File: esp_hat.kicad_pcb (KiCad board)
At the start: 2 copper layers, 73 x 30 mm, 111 parts, among them J1 U.FL, P1 CONN_02X20, U1 ESP8266EX, U2 AP1117D33, Y1 26MHz

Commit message: v0.2 fab files
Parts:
- added REF**: Symbol_OSHW-Logo_SilkScreen, Symbols:Symbol_OSHW-Logo_SilkScreen, F.Cu at (91.1, 109.5)
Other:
- board text added: "ESP8266 WiFi for Raspberry Pi v0.2 2015-12-31 by Andrew Litt https://github.com/al177/esp_hat"
- board text added: "NO STEP"
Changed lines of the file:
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@@
 (kicad_pcb (version 4) (host pcbnew 4.0.1-3.201512221401+6198~38~ubuntu15.10.1-stable)
   (general
-    (links 220)
+    (links 0)
     (no_connects 2)
     (area 56.924999 84.924999 130.075001 115.075001)
     (thickness 1.6)
-    (drawings 11)
+    (drawings 13)
     (tracks 504)
     (zones 0)
-    (modules 111)
+    (modules 112)
     (nets 30)
   )
   (page A4)
   (title_block
-    (title WiFiPiPants)
+    (title "ESP8266 WiFi for Raspberry Pi")
     (date 2015-12-31)
     (rev v0.2)
@@
       (net 1 GND))
   )
+  (module Symbols:Symbol_OSHW-Logo_SilkScreen (layer F.Cu)
+    (at 91.1 109.5)
+    (descr "Symbol, OSHW-Logo, Silk Screen,")
+    (tags "Symbol, OSHW-Logo, Silk Screen,")
+    (fp_text reference REF** (at 0.09906 -4.38912) (layer F.SilkS) hide
+      (effects (font (size 1 1) (thickness 0.15)))
+    )
+    (fp_text value Symbol_OSHW-Logo_SilkScreen (at 0.30988 6.56082) (layer F.Fab)
+      (effects (font (size 1 1) (thickness 0.15)))
+    )
+    (fp_line (start 1.66878 2.68986) (end 2.02946 4.16052) (layer F.SilkS) (width 0.15))
+    (fp_line (start 2.02946 4.16052) (end 2.30886 3.0988) (layer F.SilkS) (width 0.15))
+    (fp_line (start 2.30886 3.0988) (end 2.61874 4.17068) (layer F.SilkS) (width 0.15))
+    (fp_line (start 2.61874 4.17068) (end 2.9591 2.72034) (layer F.SilkS) (width 0.15))
+    (fp_line (start 0.24892 3.38074) (end 1.03886 3.37058) (layer F.SilkS) (width 0.15))
+    (fp_line (start 1.03886 3.37058) (end 1.04902 3.38074) (layer F.SilkS) (width 0.15))
+    (fp_line (start 1.04902 3.38074) (end 1.04902 3.37058) (layer F.SilkS) (width 0.15))
+    (fp_line (start 1.08966 2.65938) (end 1.08966 4.20116) (layer F.SilkS) (width 0.15))
+    (fp_line (start 0.20066 2.64922) (end 0.20066 4.21894) (layer F.SilkS) (width 0.15))
+    (fp_line (start 0.20066 4.21894) (end 0.21082 4.20878) (layer F.SilkS) (width 0.15))
+    (fp_line (start -0.35052 2.75082) (end -0.70104 2.66954) (layer F.SilkS) (width 0.15))
+    (fp_line (start -0.70104 2.66954) (end -1.02108 2.65938) (layer F.SilkS) (width 0.15))
+    (fp_line (start -1.02108 2.65938) (end -1.25984 2.86004) (layer F.SilkS) (width 0.15))
+    (fp_line (start -1.25984 2.86004) (end -1.29032 3.12928) (layer F.SilkS) (width 0.15))
+    (fp_line (start -1.29032 3.12928) (end -1.04902 3.37058) (layer F.SilkS) (width 0.15))
+    (fp_line (start -1.04902 3.37058) (end -0.6604 3.50012) (layer F.SilkS) (width 0.15))
+    (fp_line (start -0.6604 3.50012) (end -0.48006 3.66014) (layer F.SilkS) (width 0.15))
+    (fp_line (start -0.48006 3.66014) (end -0.43942 3.95986) (layer F.SilkS) (width 0.15))
+    (fp_line (start -0.43942 3.95986) (end -0.67056 4.18084) (layer F.SilkS) (width 0.15))
+    (fp_line (start -0.67056 4.18084) (end -0.9906 4.20878) (layer F.SilkS) (width 0.15))
+    (fp_line (start -0.9906 4.20878) (end -1.34112 4.09956) (layer F.SilkS) (width 0.15))
+    (fp_line (start -2.37998 2.64922) (end -2.6289 2.66954) (layer F.SilkS) (width 0.15))
+    (fp_line (start -2.6289 2.66954) (end -2.8702 2.91084) (layer F.SilkS) (width 0.15))
+    (fp_line (start -2.8702 2.91084) (end -2.9591 3.40106) (layer F.SilkS) (width 0.15))
+    (fp_line (start -2.9591 3.40106) (end -2.93116 3.74904) (layer F.SilkS) (width 0.15))
+    (fp_line (start -2.93116 3.74904) (end -2.7305 4.06908) (layer F.SilkS) (width 0.15))
+    (fp_line (start -2.7305 4.06908) (end -2.47904 4.191) (layer F.SilkS) (width 0.15))
+    (fp_line (start -2.47904 4.191) (end -2.16916 4.11988) (layer F.SilkS) (width 0.15))
+    (fp_line (start -2.16916 4.11988) (end -1.95072 3.93954) (layer F.SilkS) (width 0.15))
+    (fp_line (start -1.95072 3.93954) (end -1.8796 3.4798) (layer F.SilkS) (width 0.15))
+    (fp_line (start -1.8796 3.4798) (end -1.9304 3.07086) (layer F.SilkS) (width 0.15))
+    (fp_line (start -1.9304 3.07086) (end -2.03962 2.78892) (layer F.SilkS) (width 0.15))
+    (fp_line (start -2.03962 2.78892) (end -2.4003 2.65938) (layer F.SilkS) (width 0.15))
+    (fp_line (start -1.78054 0.92964) (end -2.03962 1.49098) (layer F.SilkS) (width 0.15))
+    (fp_line (start -2.03962 1.49098) (end -1.50114 2.00914) (layer F.SilkS) (width 0.15))
+    (fp_line (start -1.50114 2.00914) (end -0.98044 1.7399) (layer F.SilkS) (width 0.15))
+    (fp_line (start -0.98044 1.7399) (end -0.70104 1.89992) (layer F.SilkS) (width 0.15))
+    (fp_line (start 0.73914 1.8796) (end 1.06934 1.6891) (layer F.SilkS) (width 0.15))
+    (fp_line (start 1.06934 1.6891) (end 1.50876 2.0193) (layer F.SilkS) (width 0.15))
+    (fp_line (start 1.50876 2.0193) (end 1.9812 1.52908) (layer F.SilkS) (width 0.15))
+    (fp_line (start 1.9812 1.52908) (end 1.69926 1.04902) (layer F.SilkS) (width 0.15))
+    (fp_line (start 1.69926 1.04902) (end 1.88976 0.57912) (layer F.SilkS) (width 0.15))
+    (fp_line (start 1.88976 0.57912) (end 2.49936 0.39116) (layer F.SilkS) (width 0.15))
+    (fp_line (start 2.49936 0.39116) (end 2.49936 -0.28956) (layer F.SilkS) (width 0.15))
+    (fp_line (start 2.49936 -0.28956) (end 1.94056 -0.42926) (layer F.SilkS) (width 0.15))
+    (fp_line (start 1.94056 -0.42926) (end 1.7399 -1.00076) (layer F.SilkS) (width 0.15))
+    (fp_line (start 1.7399 -1.00076) (end 2.00914 -1.47066) (layer F.SilkS) (width 0.15))
+    (fp_line (start 2.00914 -1.47066) (end 1.53924 -1.9812) (layer F.SilkS) (width 0.15))
+    (fp_line (start 1.53924 -1.9812) (end 1.02108 -1.71958) (layer F.SilkS) (width 0.15))
+    (fp_line (start 1.02108 -1.71958) (end 0.55118 -1.92024) (layer F.SilkS) (width 0.15))
+    (fp_line (start 0.55118 -1.92024) (end 0.381 -2.46126) (layer F.SilkS) (width 0.15))
+    (fp_line (start 0.381 -2.46126) (end -0.30988 -2.47904) (layer F.SilkS) (width 0.15))
+    (fp_line (start -0.30988 -2.47904) (end -0.5207 -1.9304) (layer F.SilkS) (width 0.15))
+    (fp_line (start -0.5207 -1.9304) (end -0.9398 -1.76022) (layer F.SilkS) (width 0.15))
+    (fp_line (start -0.9398 -1.76022) (end -1.49098 -2.02946) (layer F.SilkS) (width 0.15))
+    (fp_line (start -1.49098 -2.02946) (end -2.00914 -1.50114) (layer F.SilkS) (width 0.15))
+    (fp_line (start -2.00914 -1.50114) (end -1.76022 -0.96012) (layer F.SilkS) (width 0.15))
+    (fp_line (start -1.76022 -0.96012) (end -1.9304 -0.48006) (layer F.SilkS) (width 0.15))
+    (fp_line (start -1.9304 -0.48006) (end -2.47904 -0.381) (layer F.SilkS) (width 0.15))
+    (fp_line (start -2.47904 -0.381) (end -2.4892 0.32004) (layer F.SilkS) (width 0.15))
+    (fp_line (start -2.4892 0.32004) (end -1.9304 0.5207) (layer F.SilkS) (width 0.15))
+    (fp_line (start -1.9304 0.5207) (end -1.7907 0.91948) (layer F.SilkS) (width 0.15))
+    (fp_line (start 0.35052 0.89916) (end 0.65024 0.7493) (layer F.SilkS) (width 0.15))
+    (fp_line (start 0.65024 0.7493) (end 0.8509 0.55118) (layer F.SilkS) (width 0.15))
+    (fp_line (start 0.8509 0.55118) (end 1.00076 0.14986) (layer F.SilkS) (width 0.15))
+    (fp_line (start 1.00076 0.14986) (end 1.00076 -0.24892) (layer F.SilkS) (width 0.15))
+    (fp_line (start 1.00076 -0.24892) (end 0.8509 -0.59944) (layer F.SilkS) (width 0.15))
+    (fp_line (start 0.8509 -0.59944) (end 0.39878 -0.94996) (layer F.SilkS) (width 0.15))
+    (fp_line (start 0.39878 -0.94996) (end -0.0508 -1.00076) (layer F.SilkS) (width 0.15))
+    (fp_line (start -0.0508 -1.00076) (end -0.44958 -0.89916) (layer F.SilkS) (width 0.15))
+    (fp_line (start -0.44958 -0.89916) (end -0.8509 -0.55118) (layer F.SilkS) (width 0.15))
+    (fp_line (start -0.8509 -0.55118) (end -1.00076 -0.09906) (layer F.SilkS) (width 0.15))
+    (fp_line (start -1.00076 -0.09906) (end -0.94996 0.39878) (layer F.SilkS) (width 0.15))
+    (fp_line (start -0.94996 0.39878) (end -0.70104 0.70104) (layer F.SilkS) (width 0.15))
+    (fp_line (start -0.70104 0.70104) (end -0.35052 0.89916) (layer F.SilkS) (width 0.15))
+    (fp_line (start -0.35052 0.89916) (end -0.70104 1.89992) (layer F.SilkS) (width 0.15))
+    (fp_line (start 0.35052 0.89916) (end 0.7493 1.89992) (layer F.SilkS) (width 0.15))
+  )
+  (gr_text "NO STEP" (at 60.5 97.5 90) (layer F.SilkS)
+    (effects (font (size 1.5 1.5) (thickness 0.375)))
+  )
+  (gr_text "ESP8266 WiFi for Raspberry Pi\nv0.2 2015-12-31\nby Andrew Litt\nhttps://github.com/al177/esp_hat" (at 88.01 110.82) (layer B.SilkS)
+    (effects (font (size 1 1) (thickness 0.125)) (justify right mirror))
+  )
   (gr_text "max skew must be <250mil\nvariance as routed is 235mil" (at 94.825 101.225) (layer Cmts.User)

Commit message: Add GPIO5/GPIO6 select pad, fix no-connects, remove paste on option pads
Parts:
- added P2: CH_PD, esp_hat:GS3, F.Cu at (104.5, 93.2)
- R3, R4, R5: footprint Connect:GS2 -> esp_hat:GS2
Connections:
- P1 pad 31: (no net) -> GPIO6
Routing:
- net GPIO6: track 0.00 -> 7.90 mm
- net GPIO5: track 58.7 -> 65.7 mm
- net GND: track 250.6 -> 245.7 mm, vias 56 -> 57
- net /50ohm_ant: track 0.99 -> 2.57 mm
- net /50ohm_ufl: track 0.00 -> 1.20 mm
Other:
- board text added: "GPIO0"
- board text added: "GPIO2"
- board text added: "GPIO5"
- board text added: "GPIO6"
- board text added: "MTDO"

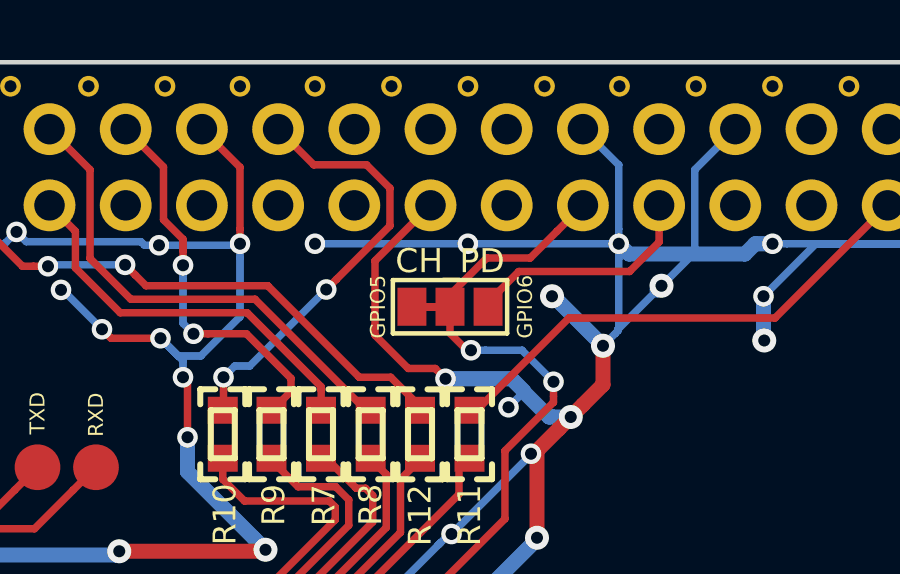
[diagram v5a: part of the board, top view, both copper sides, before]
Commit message: Change CH_PD name to CHIP_EN
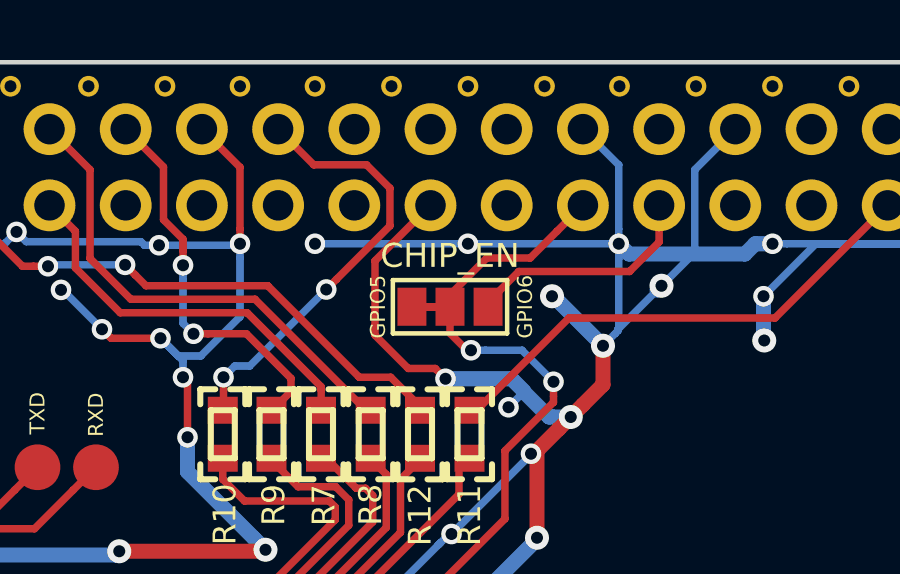
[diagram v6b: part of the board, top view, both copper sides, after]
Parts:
- P2: value CH_PD -> CHIP_EN
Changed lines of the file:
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@@
     (links 223)
     (no_connects 0)
-    (area 56.808999 79.875 134.19881 117.47626)
+    (area 56.924999 84.924999 130.075001 115.075001)
     (thickness 1.6)
     (drawings 18)
@@
     (pad_to_mask_clearance 0.2)
     (aux_axis_origin 0 0)
-    (visible_elements 7FFE7F7F)
+    (visible_elements 7FFFFF7F)
     (pcbplotparams
       (layerselection 0x010f8_80000001)
@@
       (effects (font (size 1 1) (thickness 0.15)))
     )
-    (fp_text value CH_PD (at 1.524 0 180) (layer F.SilkS)
+    (fp_text value CHIP_EN (at 1.7 0 180) (layer F.SilkS)
       (effects (font (size 0.8 0.8) (thickness 0.125)))
     )

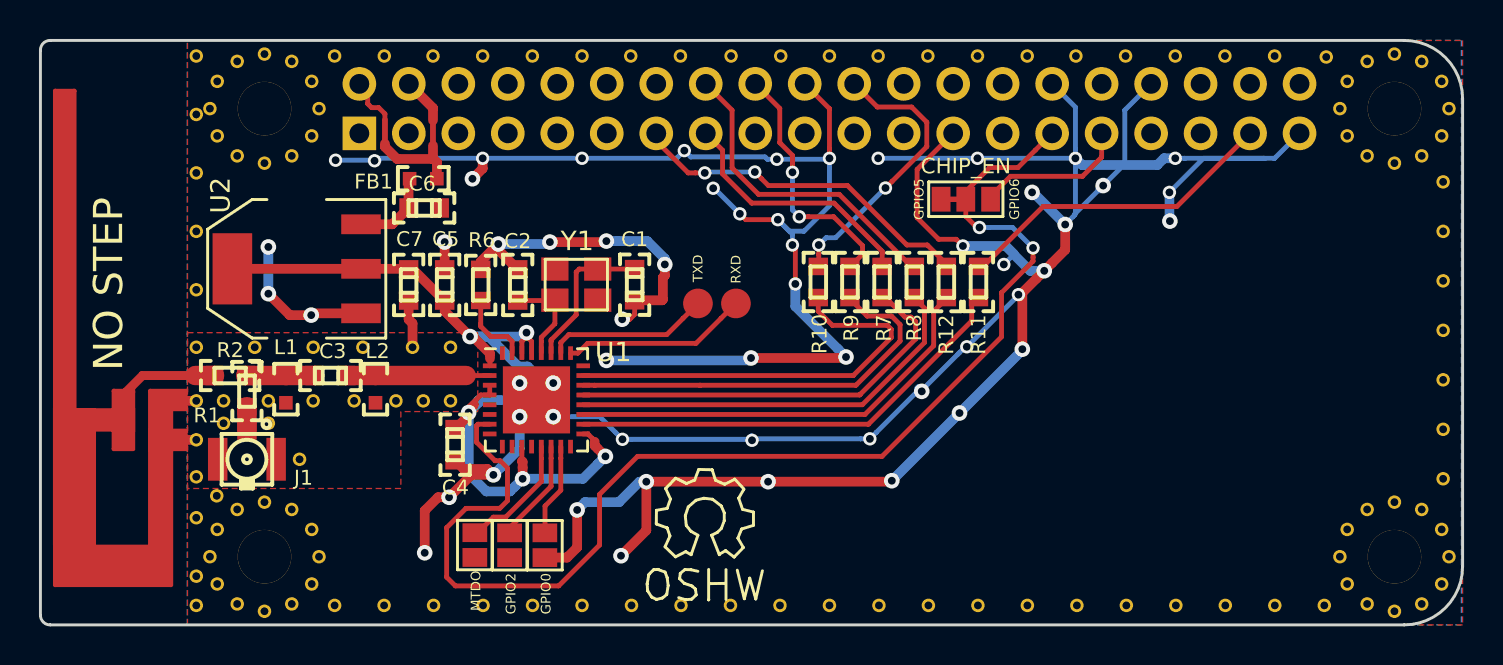
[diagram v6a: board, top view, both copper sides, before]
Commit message: Add part# parameters, clean up refs, set attributes for proper mfg
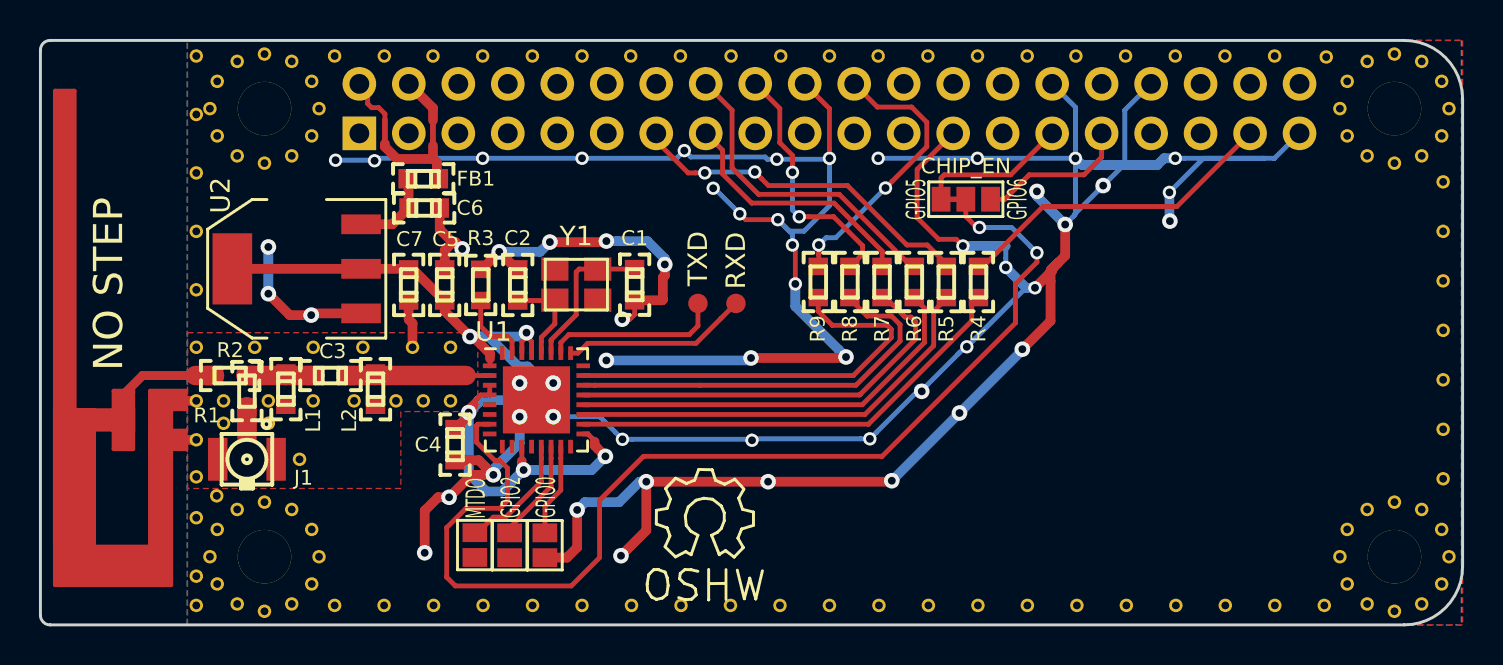
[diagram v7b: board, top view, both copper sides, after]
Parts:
- FB1, L1, L2: footprint mcuos:0603(1608m) -> mcuos:0603(1608m)-CHIP-CAP
- J1: value U.FL -> DNP
- JP2: renamed from R3; value DNP -> MTDO
- JP3: renamed from R4; value DNP -> GPIO2
- JP4: renamed from R5; value DNP -> GPIO0
- R3: renamed from R6; value 12.0K -> 12.0K 1%
- W1, W2: footprint Measurement_Points:Measurement_Point_Round-SMD-Pad_Small -> esp_hat:Measurement_Point_Round-SMD-Pad_Small
- Y1: value 26MHz -> 26MHz 10ppm
- renumbered P2 to JP1, R11 to R4, R12 to R5, R8 to R6, R9 to R8, R10 to R9
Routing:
- net GND: track 245.7 -> 248.4 mm, vias 57 -> 55
- net GPIO5: track 65.7 -> 67.6 mm
- net Net-(U1-Pad26): track 8.41 -> 9.08 mm
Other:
- net class 50ohm_oshpark: clearance 0.15 -> 0.16
- board text added: "ESP8266 WiFi for Raspberry Pi v0.2 2016-01-03 by Andrew Litt https://github.com/al177/esp_hat"
- board text removed: "ESP8266 WiFi for Raspberry Pi v0.2 2015-12-31 by Andrew Litt https://github.com/al177/esp_hat"
